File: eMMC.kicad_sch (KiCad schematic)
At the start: 18 parts, among them U1 rv1126/rv1109, U3 MTFC4GACAJCN

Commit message: updated Resistors
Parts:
- R40: LCSC (none) -> C25940; Model (none) -> 0402WGJ0472TCE; Vendor (none) -> UNI-ROYAL(厚声)
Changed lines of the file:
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@@
+      (effects (font (size 1.27 1.27)) hide)
+    )
+    (property "Description" "电阻类型: 厚膜电阻 阻值: 4.7kΩ 精度: ±5% 功率: 1/16W 温度系数: ±100ppm/℃ 最大工作电压: 50V 工作温" (at 99.06 157.48 0)
+      (effects (font (size 1.27 1.27)) hide)
+    )
+    (property "LCSC" "C25940" (at 99.06 157.48 0)
+      (effects (font (size 1.27 1.27)) hide)
+    )
+    (property "Model" "0402WGJ0472TCE" (at 99.06 157.48 0)
+      (effects (font (size 1.27 1.27)) hide)
+    )
+    (property "Vendor" "UNI-ROYAL(厚声)" (at 99.06 157.48 0)
       (effects (font (size 1.27 1.27)) hide)
     )
@@
       (effects (font (size 1.27 1.27)) hide)
     )
+    (property "Description" "电阻类型: 厚膜电阻 阻值: 4.7kΩ 精度: ±5% 功率: 1/16W 温度系数: ±100ppm/℃ 最大工作电压: 50V 工作温" (at 99.06 180.34 0)
+      (effects (font (size 1.27 1.27)) hide)
+    )
+    (property "LCSC" "C25940" (at 99.06 180.34 0)
+      (effects (font (size 1.27 1.27)) hide)
+    )
+    (property "Model" "0402WGJ0472TCE" (at 99.06 180.34 0)
+      (effects (font (size 1.27 1.27)) hide)
+    )
+    (property "Vendor" "UNI-ROYAL(厚声)" (at 99.06 180.34 0)
+      (effects (font (size 1.27 1.27)) hide)
+    )
     (pin "1")
     (pin "2")
@@
       (effects (font (size 1.27 1.27)) hide)
     )
+    (property "Description" "电阻类型: 厚膜电阻 阻值: 4.7kΩ 精度: ±5% 功率: 1/16W 温度系数: ±100ppm/℃ 最大工作电压: 50V 工作温" (at 181.61 138.43 0)
+      (effects (font (size 1.27 1.27)) hide)
+    )
+    (property "LCSC" "C25940" (at 181.61 138.43 0)
+      (effects (font (size 1.27 1.27)) hide)
+    )
+    (property "Model" "0402WGJ0472TCE" (at 181.61 138.43 0)
+      (effects (font (size 1.27 1.27)) hide)
+    )
+    (property "Vendor" "UNI-ROYAL(厚声)" (at 181.61 138.43 0)
+      (effects (font (size 1.27 1.27)) hide)
+    )
     (pin "1")
     (pin "2")
@@
       (effects (font (size 1.27 1.27)) hide)
     )
+    (property "Description" "电阻类型: 厚膜电阻 阻值: 4.7kΩ 精度: ±5% 功率: 1/16W 温度系数: ±100ppm/℃ 最大工作电压: 50V 工作温" (at 134.62 138.43 0)
+      (effects (font (size 1.27 1.27)) hide)
+    )
+    (property "LCSC" "C25940" (at 134.62 138.43 0)
+      (effects (font (size 1.27 1.27)) hide)
+    )
+    (property "Model" "0402WGJ0472TCE" (at 134.62 138.43 0)
+      (effects (font (size 1.27 1.27)) hide)
+    )
+    (property "Vendor" "UNI-ROYAL(厚声)" (at 134.62 138.43 0)
+      (effects (font (size 1.27 1.27)) hide)
+    )

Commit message: added missing pins
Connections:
- no-connect marks 5 -> 6
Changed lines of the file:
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@@
   (no_connect (at 101.6 69.85))
   (no_connect (at 101.6 80.01))
+  (no_connect (at 163.83 44.45))
   (wire (pts (xy 134.62 130.81) (xy 134.62 134.62))
     (stroke (width 0) (type default))

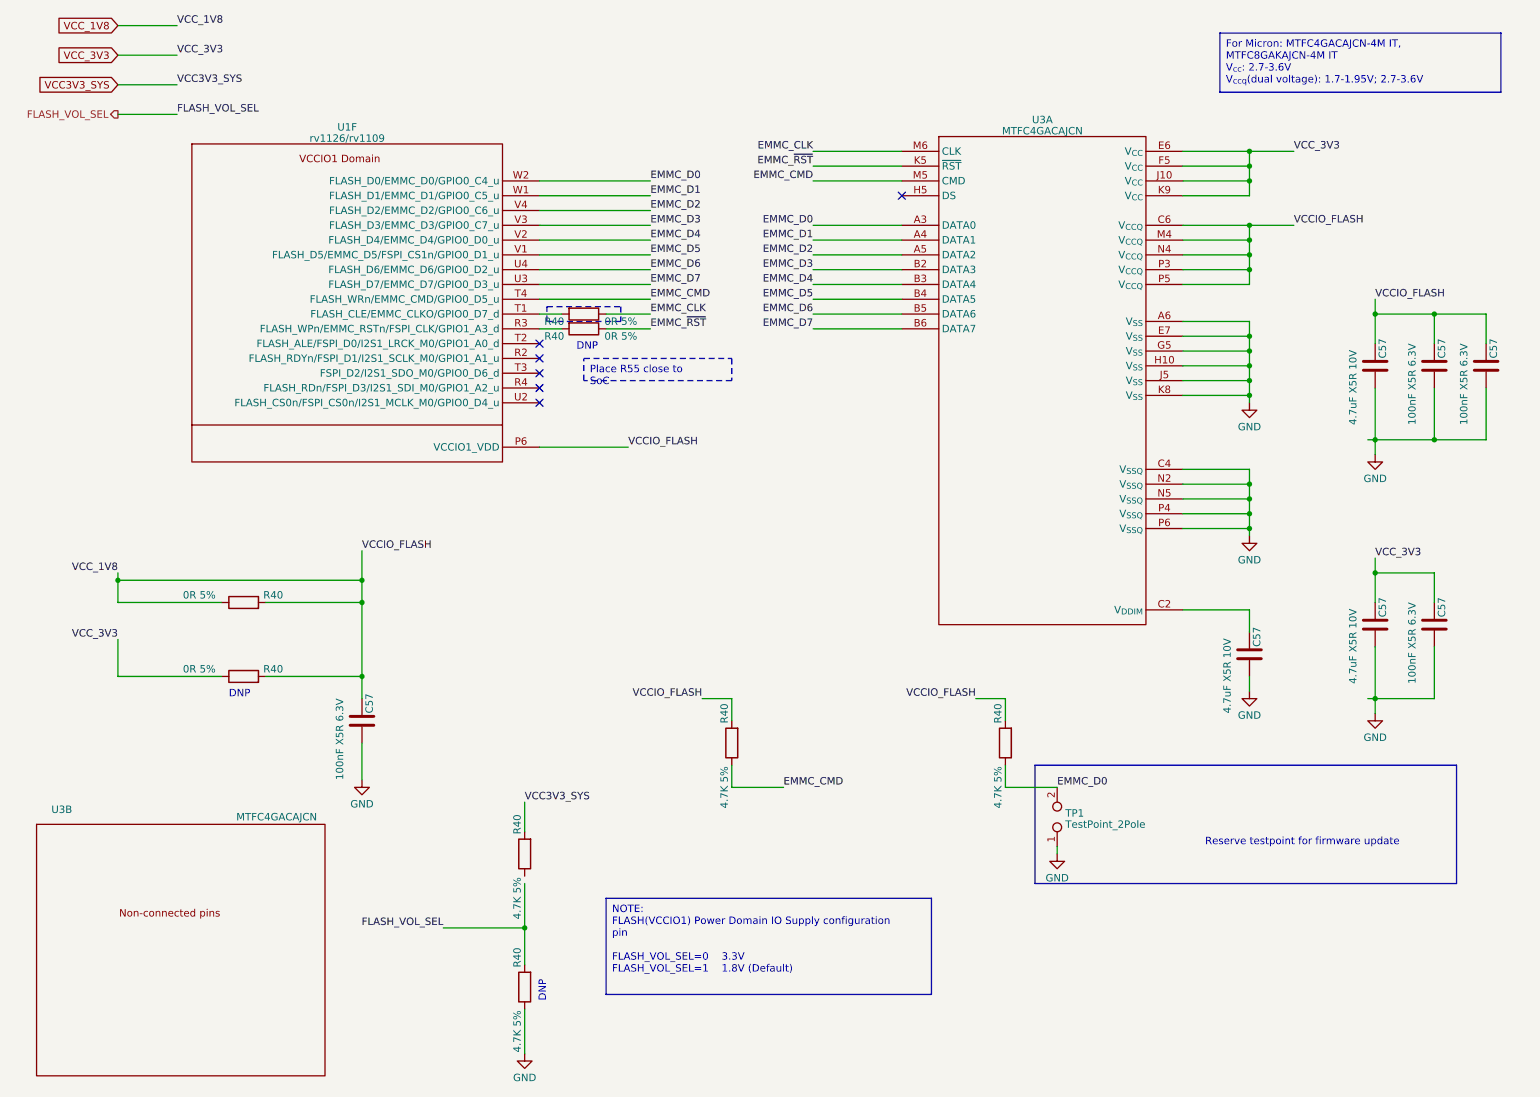
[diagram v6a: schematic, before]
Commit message: fix some ERCs
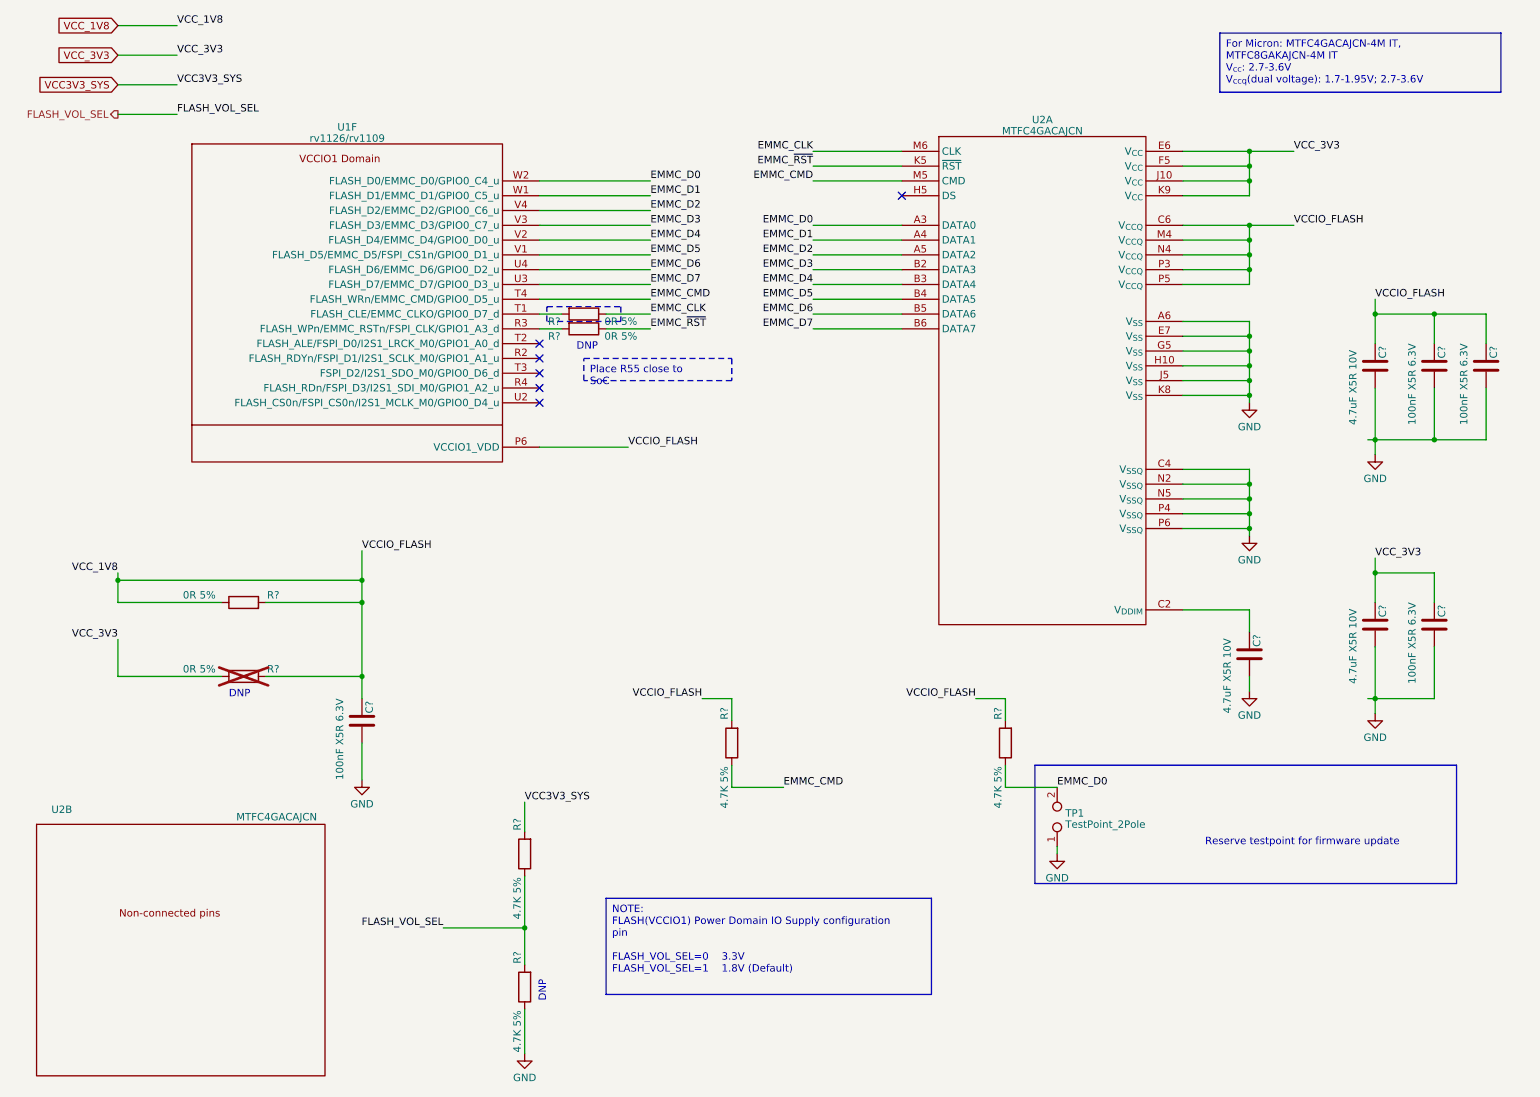
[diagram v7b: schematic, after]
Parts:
- R?: renamed from R40; now not fitted
- renumbered C57 to C?, R40 to R?, U3 to U2
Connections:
- net FLASH_VOL_SEL: now also R?.1

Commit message: updated symbols
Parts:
- R? (x4): LCSC (none) -> C17168; Model (none) -> 0402WGF0000TCE; Vendor (none) -> UNI-ROYAL(厚声)
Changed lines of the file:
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@@
+      (effects (font (size 1.27 1.27)) hide)
+    )
+    (property "Description" "电阻类型: 厚膜电阻 阻值: 0Ω 精度: ±1% 功率: 1/16W 温度系数: ±800ppm/℃ 最大工作电压: 50V 工作" (at 109.22 67.31 0)
+      (effects (font (size 1.27 1.27)) hide)
+    )
+    (property "LCSC" "C17168" (at 109.22 67.31 0)
+      (effects (font (size 1.27 1.27)) hide)
+    )
+    (property "Model" "0402WGF0000TCE" (at 109.22 67.31 0)
+      (effects (font (size 1.27 1.27)) hide)
+    )
+    (property "Vendor" "UNI-ROYAL(厚声)" (at 109.22 67.31 0)
       (effects (font (size 1.27 1.27)) hide)
     )
@@
     )
     (property "Datasheet" "~" (at 50.8 114.3 0)
+      (effects (font (size 1.27 1.27)) hide)
+    )
+    (property "Description" "电阻类型: 厚膜电阻 阻值: 0Ω 精度: ±1% 功率: 1/16W 温度系数: ±800ppm/℃ 最大工作电压: 50V 工作" (at 50.8 114.3 0)
+      (effects (font (size 1.27 1.27)) hide)
+    )
+    (property "LCSC" "C17168" (at 50.8 114.3 0)
+      (effects (font (size 1.27 1.27)) hide)
+    )
+    (property "Model" "0402WGF0000TCE" (at 50.8 114.3 0)
+      (effects (font (size 1.27 1.27)) hide)
+    )
+    (property "Vendor" "UNI-ROYAL(厚声)" (at 50.8 114.3 0)
       (effects (font (size 1.27 1.27)) hide)
     )
@@
       (effects (font (size 1.27 1.27)) hide)
     )
+    (property "Description" "电阻类型: 厚膜电阻 阻值: 0Ω 精度: ±1% 功率: 1/16W 温度系数: ±800ppm/℃ 最大工作电压: 50V 工作" (at 50.8 127 0)
+      (effects (font (size 1.27 1.27)) hide)
+    )
+    (property "LCSC" "C17168" (at 50.8 127 0)
+      (effects (font (size 1.27 1.27)) hide)
+    )
+    (property "Model" "0402WGF0000TCE" (at 50.8 127 0)
+      (effects (font (size 1.27 1.27)) hide)
+    )
+    (property "Vendor" "UNI-ROYAL(厚声)" (at 50.8 127 0)
+      (effects (font (size 1.27 1.27)) hide)
+    )
     (pin "1")
     (pin "2")
@@
     )
     (property "Datasheet" "~" (at 109.22 64.77 0)
+      (effects (font (size 1.27 1.27)) hide)
+    )
+    (property "Description" "电阻类型: 厚膜电阻 阻值: 0Ω 精度: ±1% 功率: 1/16W 温度系数: ±800ppm/℃ 最大工作电压: 50V 工作" (at 109.22 64.77 0)
+      (effects (font (size 1.27 1.27)) hide)
+    )
+    (property "LCSC" "C17168" (at 109.22 64.77 0)
+      (effects (font (size 1.27 1.27)) hide)
+    )
+    (property "Model" "0402WGF0000TCE" (at 109.22 64.77 0)
+      (effects (font (size 1.27 1.27)) hide)
+    )
+    (property "Vendor" "UNI-ROYAL(厚声)" (at 109.22 64.77 0)
       (effects (font (size 1.27 1.27)) hide)
     )
@@
     (pin "AA3")
     (pin "R9")
+    (pin "T8")
     (pin "U7")
     (pin "V6")
@@
     (pin "W5")
     (pin "W6")
+    (pin "W7")
     (pin "Y4")
     (pin "Y5")
@@
     (pin "E20")
     (pin "F19")
-    (pin "F19")
     (pin "F20")
